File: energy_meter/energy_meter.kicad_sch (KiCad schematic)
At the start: 163 parts, among them IC1 ADUM4151BRIZ, IC2 ADUM6404ARIZ, IC3 ADP122AUJZ-3.3-R7, IC4 24LC32A_SN, IC5 ADP122AUJZ-3.3-R7, J1 Screw_Terminal_01x02, J10 EARTH, J2 Screw_Terminal_01x02, J3 MicroUSB, J4 XT30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

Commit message: Add pdf of schematic
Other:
- removed sheet central_unit
- added sheet Central unit (central.kicad_sch)
- note added: "3V3 <- 5V <----- 5V <- 3V3"
- note added: "Active low"
- note added: "All grounds (GND, AGND, DGND, REFGND) supposed to be connected here. Instead, the same GND has been used for all"
- note added: "Both screw terminal input and on-board CT mounting holes"
- note added: "Both screw terminals and banana cliff connectors"
- note added: "Decoupling capacitors added as per datasheet recommendations (Pin function descriptions, Pg 10-11)"
- note added: "Generate 3V3 for ADE9000"
- note added: "Level shifter and buffer"
- note added: "LiPo Power"
- note added: "MicroUSB/SMPS 5V Power"
- note added: "Optional EEPROM since RPi Pico already has 2MB of flash"
- note added: "Power can come from microUSB or from an SMPS getting AC power from the socket we are monitoring"
- note added: "SPI and status signal test points"
- note removed: "----->"
- note removed: "3V3 <- 5V <----- 5V <- 3V3 Why?"
- note removed: "Do we need this with RPi Pico having 2MB flash?"
- note removed: "If we provide just 3.3V here, the buffer will produce outputs at 3.3V logic. This can then be fed to the isolator"
- note removed: "Level shifter"
- note removed: "This device can operate at either 3.3V or 5V supply. It can either do 5 -> 5 or 5 -> 3.3 or 3.3 -> 3.3"
- note removed: "What should this connector be?"
- company: (none) -> Group TUE-01, EE344 \nAutodialing alarm system for temperature and humidity monitoring\n\n\n\n
- title: (none) -> Sensing unit
- moved on the sheet: BZ1, C36, C39, C40, C41, C42, C43, C44, C45, C46, C47, C48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

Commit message: Example code
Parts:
- J10: value EARTH -> IB_in
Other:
- removed sheet Central unit
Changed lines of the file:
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@@
       (effects (font (size 1.27 1.27)) (justify left))
     )
-    (property "Value" "EARTH" (at 52.07 123.19 0)
+    (property "Value" "IB_in" (at 52.07 123.19 0)
       (effects (font (size 1.27 1.27)) (justify left))
     )
@@
       )
     )
-  )
-  (sheet (at 626.11 31.75) (size 452.12 334.01) (fields_autoplaced)
-    (stroke (width 0.1524) (type solid))
-    (fill (color 0 0 0 0.0000))
-    (property "Sheetname" "Central unit" (at 626.11 31.0384 0)
-      (effects (font (size 1.27 1.27)) (justify left bottom))
-    )
-    (property "Sheetfile" "central.kicad_sch" (at 626.11 366.3446 0)
-      (effects (font (size 1.27 1.27)) (justify left top))
-    )
-    (instances
-      (project "energy_meter"
-        (path "/911e1b35-25a5-4acc-afe7-a5e849f2ebf2" (page "2"))
-      )
-    )

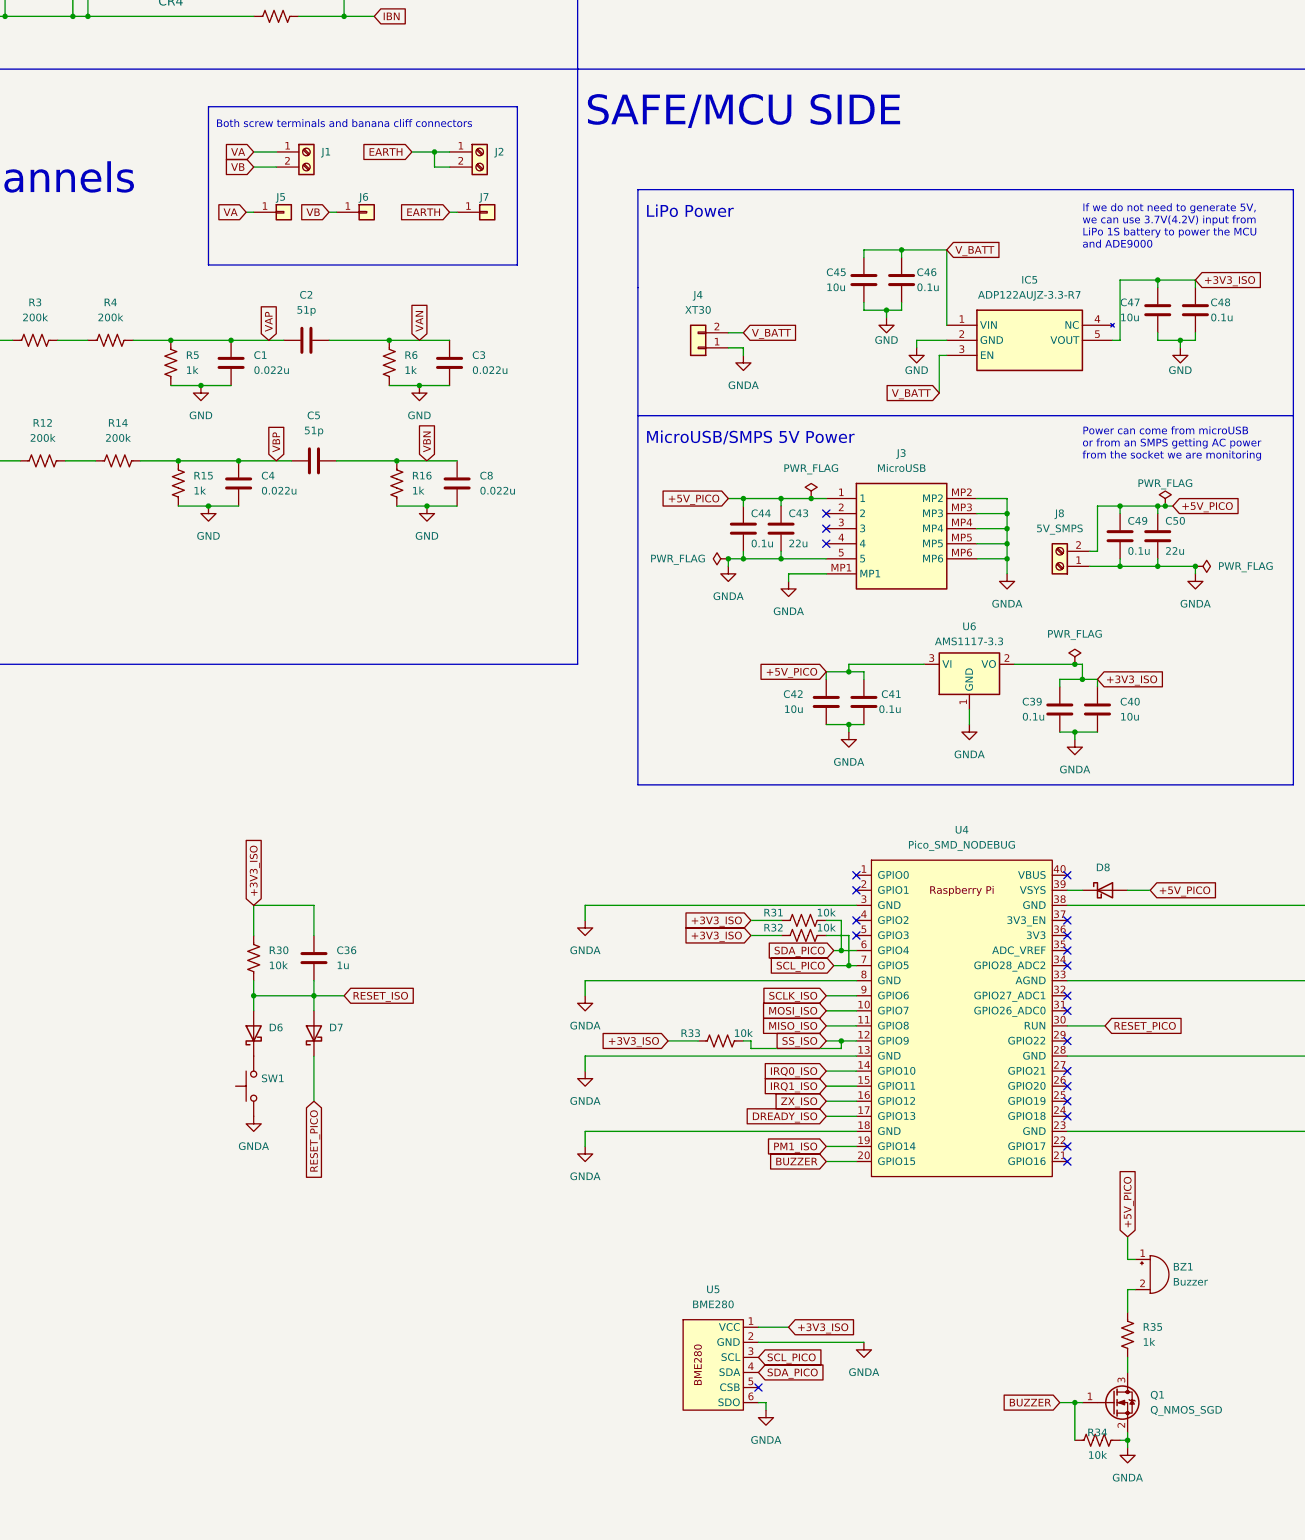
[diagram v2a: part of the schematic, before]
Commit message: Remove banana cliffs
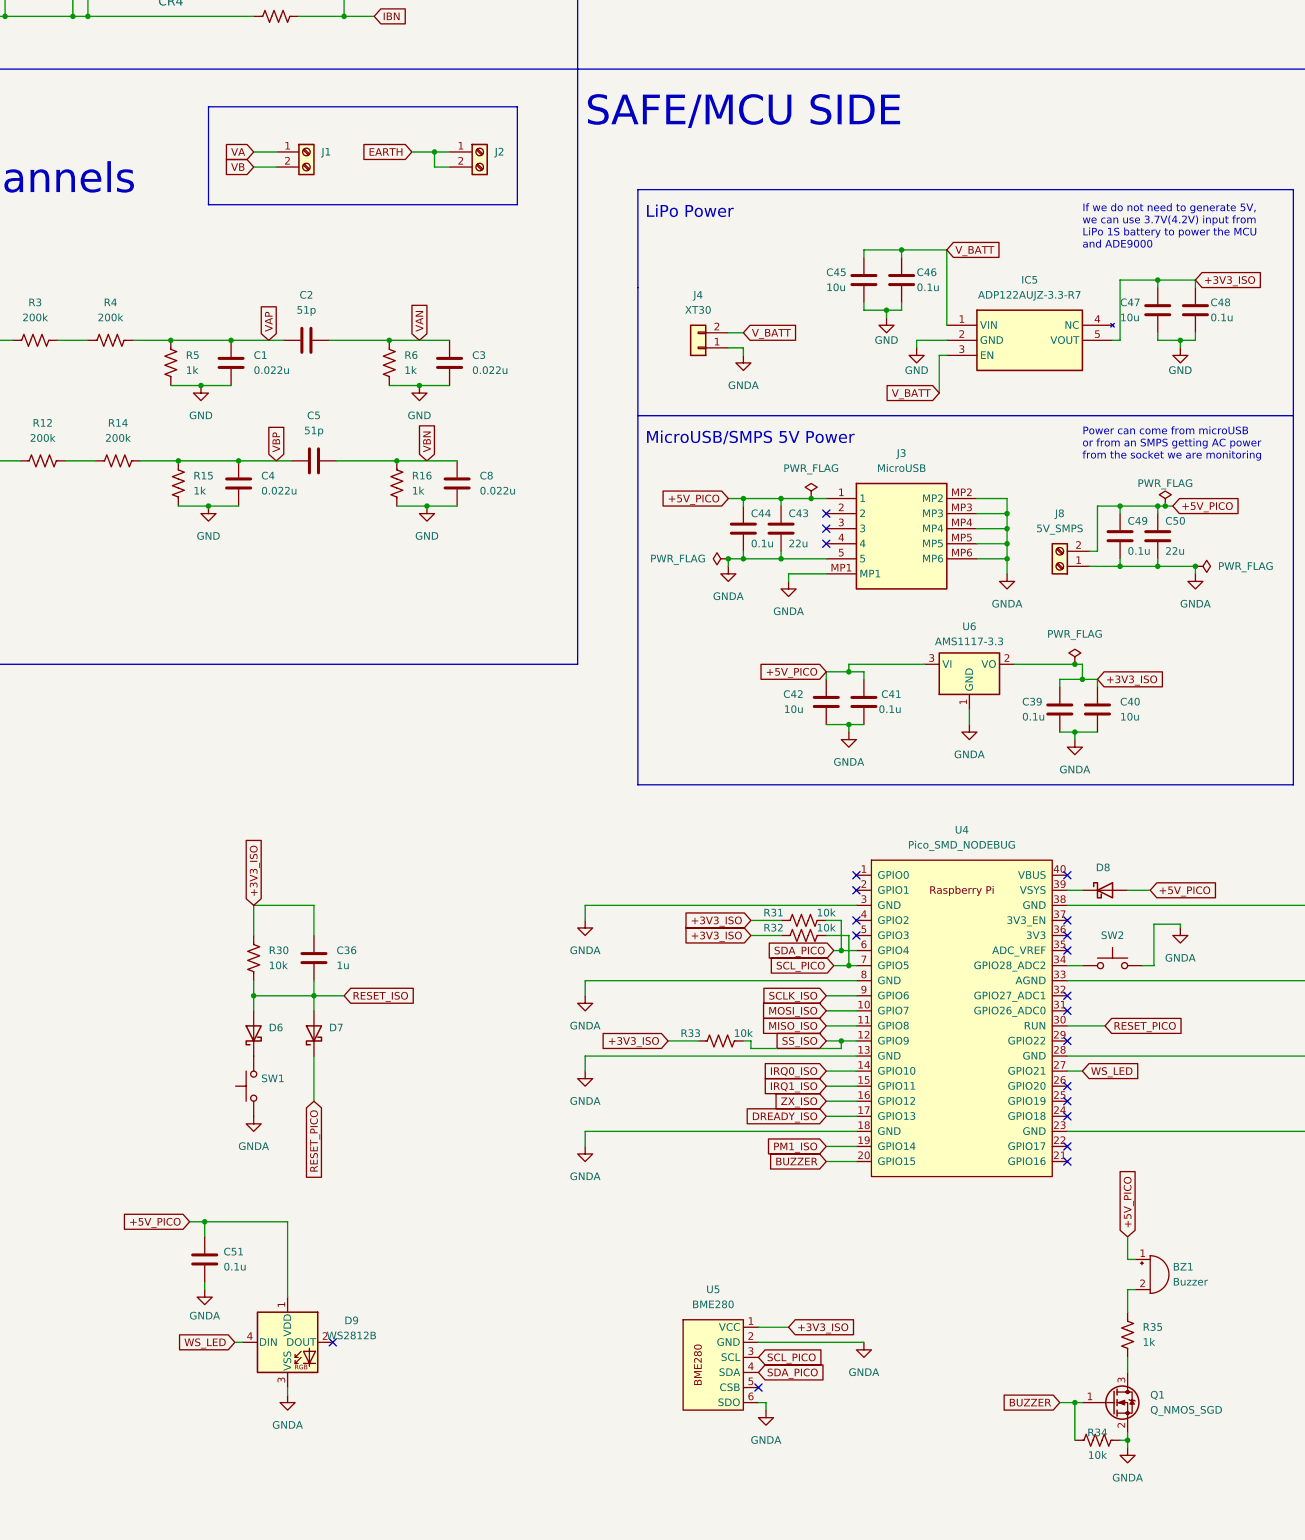
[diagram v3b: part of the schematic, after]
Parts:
- removed J5: VA, Connector:Banana_Cliff_FCR7350R_S16N-PC_Horizontal, symbol Connector_Generic:Conn_01x01
- removed J6: VB, Connector:Banana_Cliff_FCR7350R_S16N-PC_Horizontal, symbol Connector_Generic:Conn_01x01
- removed J7: EARTH, Connector:Banana_Cliff_FCR7350B_S16N-PC_Horizontal, symbol Connector_Generic:Conn_01x01
- added C51: 0.1u, Capacitor_SMD:C_0805_2012Metric_Pad1.18x1.45mm_HandSolder, symbol Device:C
- added D9: WS2812B, LED_SMD:LED_WS2812B_PLCC4_5.0x5.0mm_P3.2mm, symbol LED:WS2812B
- added SW2: SW_Push, Button_Switch_THT:SW_PUSH_6mm, symbol Switch:SW_Push
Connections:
- net +5V_PICO: now also C51.1, D9.1 (VDD)
- net GNDA: now also C51.2, D9.3 (VSS), SW2.2
- net WS_LED: now reaches U4.27 (GPIO21)
- net WS_LED: now also D9.4 (DIN)
- net at U4.34 (GPIO28_ADC2): now also SW2.1
- no-connect marks 33 -> 32
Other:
- note removed: "Both screw terminals and banana cliff connectors"

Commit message: Basic layout
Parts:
- removed C45, C47: 10u, Capacitor_SMD:C_0805_2012Metric_Pad1.18x1.45mm_HandSolder, symbol Device:C
- removed C46, C48: 0.1u, Capacitor_SMD:C_0805_2012Metric_Pad1.18x1.45mm_HandSolder, symbol Device:C
- removed IC5: ADP122AUJZ-3.3-R7, ADP122AUJZ-3.3-R7:SOT95P280X100-5N, symbol ADP122AUJZ-3.3-R7:ADP122AUJZ-3.3-R7
- removed J4: XT30, Connector_AMASS:AMASS_XT30PW-M_1x02_P2.50mm_Horizontal, symbol Connector_Generic:Conn_01x02
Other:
- note removed: "If we do not need to generate 5V, we can use 3.7V(4.2V) input from LiPo 1S battery to power the MCU and ADE9000"
- note removed: "LiPo Power"
- moved on the sheet: U5

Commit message: finished layout
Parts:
- removed TP18, TP2, TP20, TP22, TP24, TP4, TP6, TP8: TestPoint, TestPoint:TestPoint_Pad_D1.5mm, symbol Connector:TestPoint

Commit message: Restore libraries
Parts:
- U1: footprint ade9000:ADE9000ACPZ_ADI-M -> ADE9000:ADE9000ACPZ_ADI
- U2, U3: footprint SN74LV4T125PWR:PW0014A_N -> SN74LV:PW0014A_N
- U4: footprint RPi Pico:RPi_PicoW_SMD -> RPi_Pico:RPi_PicoW_SMD
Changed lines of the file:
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@@
       (effects (font (size 1.27 1.27)))
     )
-    (property "Footprint" "RPi Pico:RPi_PicoW_SMD" (at 224.79 320.04 90)
+    (property "Footprint" "RPi_Pico:RPi_PicoW_SMD" (at 224.79 320.04 90)
       (effects (font (size 1.27 1.27)) hide)
     )
@@
       (effects (font (size 1.524 1.524)))
     )
-    (property "Footprint" "SN74LV4T125PWR:PW0014A_N" (at 351.79 248.92 0)
+    (property "Footprint" "SN74LV:PW0014A_N" (at 351.79 248.92 0)
       (effects (font (size 1.27 1.27) italic) hide)
     )
@@
       (effects (font (size 1.524 1.524)))
     )
-    (property "Footprint" "SN74LV4T125PWR:PW0014A_N" (at 529.59 248.92 0)
+    (property "Footprint" "SN74LV:PW0014A_N" (at 529.59 248.92 0)
       (effects (font (size 1.27 1.27) italic) hide)
     )
@@
       (effects (font (size 1.524 1.524)))
     )
-    (property "Footprint" "ade9000:ADE9000ACPZ_ADI-M" (at 241.3 68.58 0)
+    (property "Footprint" "ADE9000:ADE9000ACPZ_ADI" (at 241.3 68.58 0)
       (effects (font (size 1.27 1.27) italic) hide)
     )

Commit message: more libraries
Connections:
- net MISO_ISO: now also U4.21 (GPIO16); no longer U4.11 (GPIO8)
- net MOSI_ISO: now also U4.25 (GPIO19); no longer U4.10 (GPIO7)
- net RESET_ISO: now also U4.26 (GPIO20)
- net SCLK_ISO: now also U4.24 (GPIO18); no longer U4.9 (GPIO6)
- net SS_ISO: now also U4.22 (GPIO17); no longer U4.12 (GPIO9)
- net WS_LED: now also U4.12 (GPIO9); no longer U4.27 (GPIO21)
- no-connect marks 32 -> 27
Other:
- moved on the sheet: BZ1, Q1, R34, R35

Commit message: pcb routing1
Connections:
- no-connect marks 27 -> 31
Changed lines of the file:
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@@
   (no_connect (at 242.57 308.61))
   (no_connect (at 36.83 69.85))
+  (no_connect (at 207.01 316.23))
   (no_connect (at 242.57 295.91))
   (no_connect (at 36.83 133.35))
@@
   (no_connect (at 187.96 382.27))
   (no_connect (at 207.01 303.53))
+  (no_connect (at 207.01 318.77))
   (no_connect (at 322.58 114.3))
   (no_connect (at 201.93 237.49))
@@
   (no_connect (at 207.01 298.45))
   (no_connect (at 424.18 199.39))
+  (no_connect (at 207.01 321.31))
+  (no_connect (at 242.57 328.93))
   (wire (pts (xy 205.74 306.07) (xy 205.74 311.15))
     (stroke (width 0) (type default))
